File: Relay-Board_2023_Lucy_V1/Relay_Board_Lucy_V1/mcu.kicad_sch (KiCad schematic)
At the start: 34 parts, among them J6 SWD_HEADER, J7 USB_B_Micro, J8 Conn_02x14_Top_Bottom, J9 DE9_Receptacle_MountingHoles, SW1 PTS815 SJM 250 SMTR LFS, SW2 PTS815 SJM 250 SMTR LFS, U10 STM32F446RETx, U7 LD39050PU33R, U9 MCP2542FD-E/SN, X1 OXETDLJANF-8MHZ

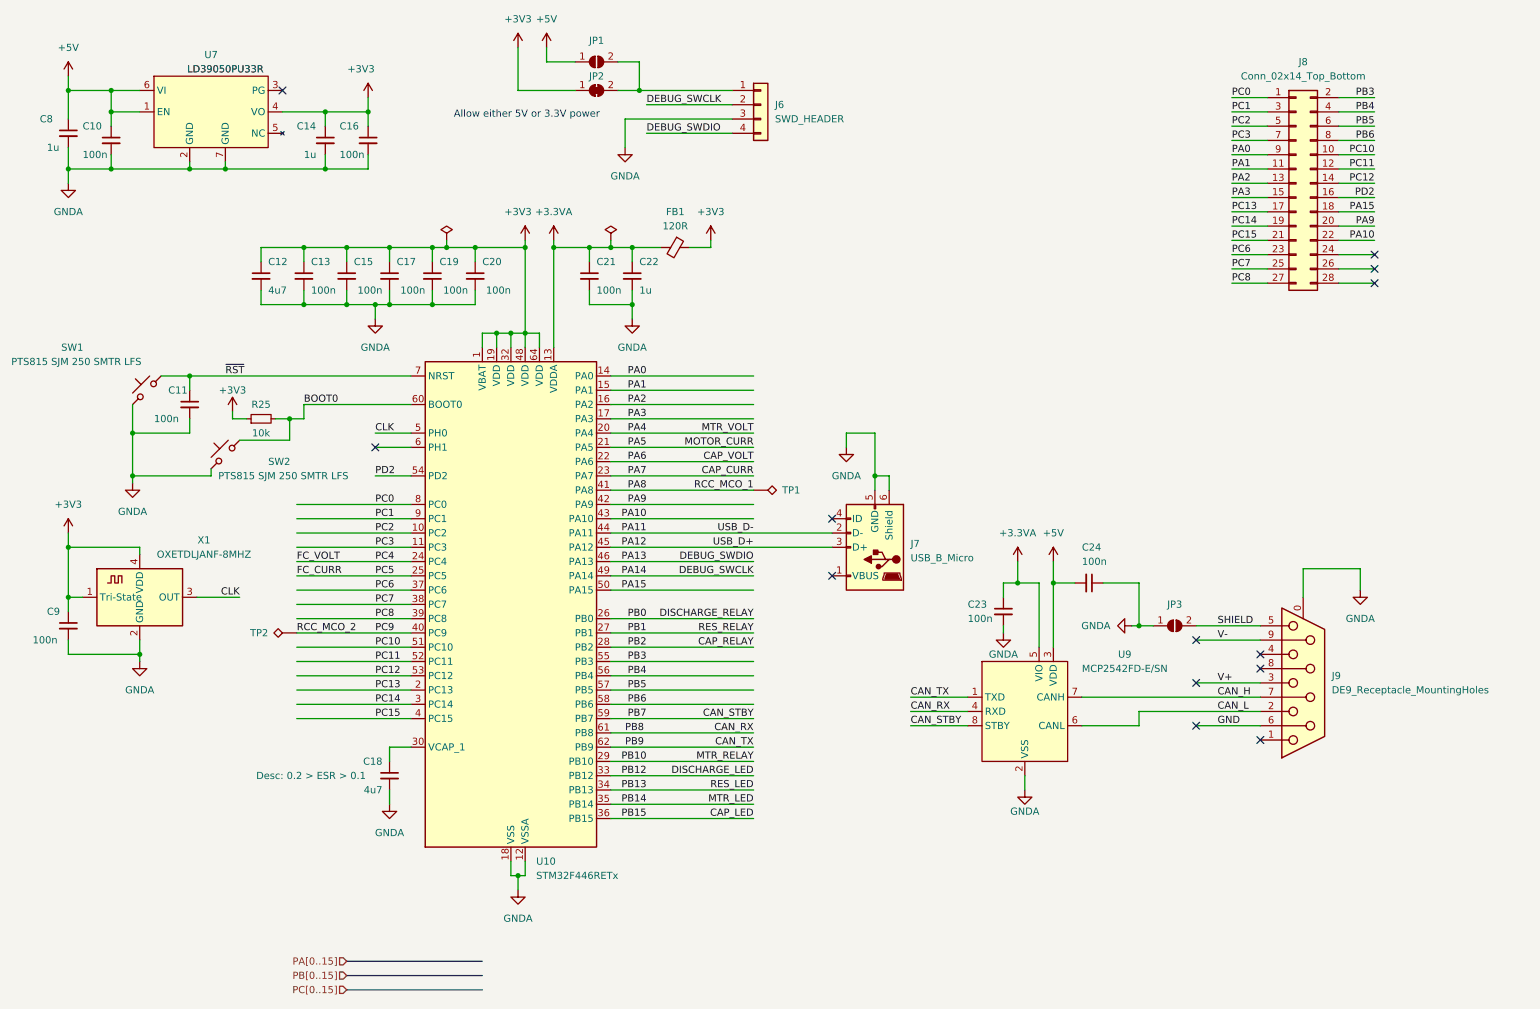
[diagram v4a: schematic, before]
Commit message: Board layout is done and routed
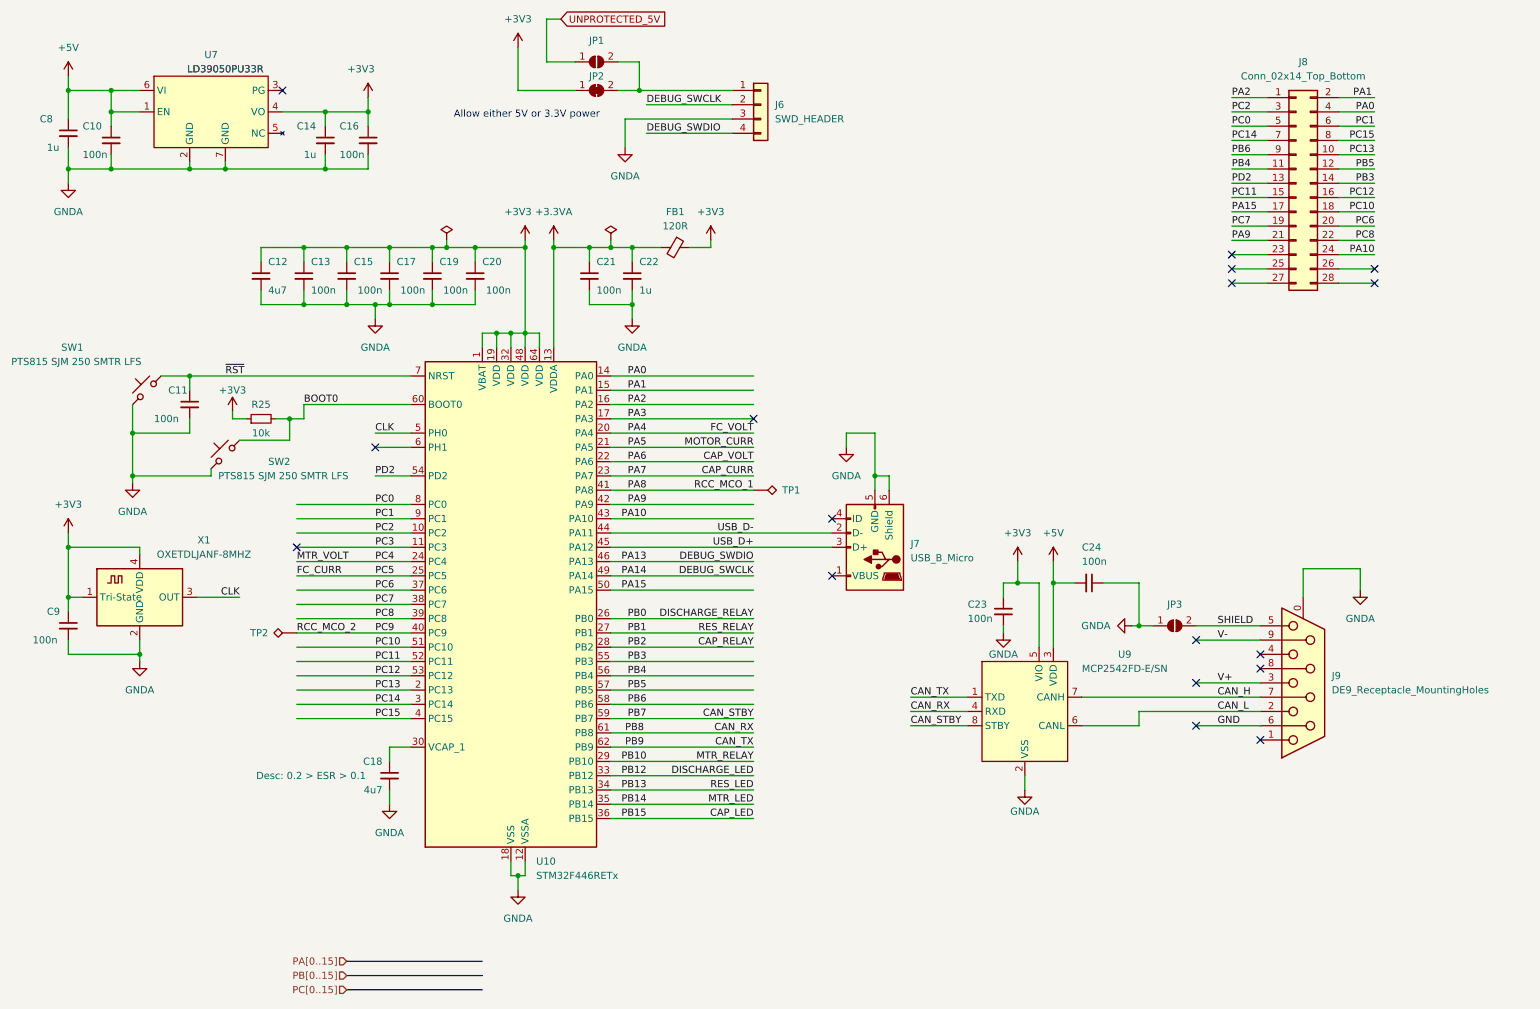
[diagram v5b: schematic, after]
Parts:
- SW2: footprint Inductor_SMD:L_1206_3216Metric -> Button_Switch_SMD:SW_SPST_PTS810
- TP1, TP2: footprint TestPoint:TestPoint_THTPad_D2.0mm_Drill1.0mm -> TestPoint:TestPoint_Pad_1.0x1.0mm
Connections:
- net +3.3VA: no longer C23.1, U9.5 (VIO)
- net +3V3: now also C23.1, U9.5 (VIO)
- net +5V: no longer JP1.1 (A)
- net FC_VOLT: now also U10.20 (PA4); no longer U10.24 (PC4)
- net MTR_VOLT: now also U10.24 (PC4); no longer U10.20 (PA4)
- net PA0: now also J8.4 (Pin_4); no longer J8.9 (Pin_9)
- net PA1: now also J8.2 (Pin_2); no longer J8.11 (Pin_11)
- net PA10: now also J8.24 (Pin_24); no longer J8.22 (Pin_22)
- net PA15: now also J8.17 (Pin_17); no longer J8.18 (Pin_18)
- net PA2: now also J8.1 (Pin_1); no longer J8.13 (Pin_13)
- net PA3: no longer J8.15 (Pin_15)
- net PA9: now also J8.21 (Pin_21); no longer J8.20 (Pin_20)
- net PB3: now also J8.14 (Pin_14); no longer J8.2 (Pin_2)
- net PB4: now also J8.11 (Pin_11); no longer J8.4 (Pin_4)
- net PB5: now also J8.12 (Pin_12); no longer J8.6 (Pin_6)
- net PB6: now also J8.9 (Pin_9); no longer J8.8 (Pin_8)
- net PC0: now also J8.5 (Pin_5); no longer J8.1 (Pin_1)
- net PC1: now also J8.6 (Pin_6); no longer J8.3 (Pin_3)
- net PC10: now also J8.18 (Pin_18); no longer J8.10 (Pin_10)
- net PC11: now also J8.15 (Pin_15); no longer J8.12 (Pin_12)
- net PC12: now also J8.16 (Pin_16); no longer J8.14 (Pin_14)
- net PC13: now also J8.10 (Pin_10); no longer J8.17 (Pin_17)
- net PC14: now also J8.7 (Pin_7); no longer J8.19 (Pin_19)
- net PC15: now also J8.8 (Pin_8); no longer J8.21 (Pin_21)
- net PC2: now also J8.3 (Pin_3); no longer J8.5 (Pin_5)
- net PC3: no longer J8.7 (Pin_7)
- net PC6: now also J8.20 (Pin_20); no longer J8.23 (Pin_23)
- net PC7: now also J8.19 (Pin_19); no longer J8.25 (Pin_25)
- net PC8: now also J8.22 (Pin_22); no longer J8.27 (Pin_27)
- net PD2: now also J8.13 (Pin_13); no longer J8.16 (Pin_16)
- net PA11 renamed USB_D-
- net PA12 renamed USB_D+
- new net UNPROTECTED_5V: JP1.1 (A)
- no-connect marks 13 -> 17

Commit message: $
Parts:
- added R34: 120, Resistor_SMD:R_0603_1608Metric, symbol Device:R_Small
- C18: Desc 0.2 > ESR > 0.1 -> ESR > 1
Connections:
- net CAN_H: now also R34.2
- net CAN_L: now also R34.1
- net GNDA: now also J8.25 (Pin_25), J8.27 (Pin_27)
- net UNPROTECTED_12V: now reaches J8.26 (Pin_26)
- net UNPROTECTED_12V: now also J8.28 (Pin_28)
- no-connect marks 17 -> 13
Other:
- moved on the sheet: C23

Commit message: Started work on the BOM file and I updated the lower current relays to work with 50A models
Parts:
- C10, C11, C13, C15, C16, C17, C19, C20, C21, C23, C24, C9: Part# (none) -> C88219
- C12: Part# (none) -> C108342
- C14, C22, C8: Part# (none) -> C77049
- C18, FB1, J7, J9: Part# (none) -> digikey
- J6, J8, JP1, JP2, JP3, TP1, TP2: Part# (none) -> N/A
- R25: Part# (none) -> C25804
- R34: Part# (none) -> C22787
- SW1, SW2: Part# (none) -> C2689510
- U10: Part# (none) -> C69336
- U7: Part# (none) -> C132827
- U9: Part# (none) -> C220598

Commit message: updated, created gerbers, created p&p, created BOM's
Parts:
- C18: Desc ESR > 1 -> ESR < 1; Part# digikey -> C108342
- FB1: value 120R -> 300R; Part# digikey -> 541-2283-1-ND
- J7: footprint Connector_USB:USB_Micro-B_Wuerth_629105150521 -> RB_FTP:USB_Micro-B_Wuerth_629105150521; Part# digikey -> 732-5960-1-ND
- J8, JP1, JP2: now left out of the parts list
- J9: Part# digikey -> N/A
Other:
- note added: "FB1: - 300 Ohms @ 100MHz - DCR 300 mOhms"
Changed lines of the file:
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@@
+    (effects (font (size 1.27 1.27)) (justify left bottom))
+  )
+  (text "FB1:\n - 300 Ohms @ 100MHz\n - DCR 300 mOhms" (at 134.62 66.04 0)
     (effects (font (size 1.27 1.27)) (justify left bottom))
   )
@@
   )
   (symbol (lib_id "Jumper:SolderJumper_2_Bridged") (at 120.65 27.94 0) (unit 1)
-    (in_bom yes) (on_board yes) (dnp no)
+    (in_bom no) (on_board yes) (dnp no)
     (property "Reference" "JP2" (at 120.65 25.4 0)
       (effects (font (size 1.27 1.27)))
@@
       (effects (font (size 1.27 1.27)) hide)
     )
-    (property "Part#" "digikey" (at 246.38 133.35 0)
+    (property "Part#" "N/A" (at 246.38 133.35 0)
       (effects (font (size 1.27 1.27)) hide)
     )
@@
       (effects (font (size 1.27 1.27)) hide)
     )
-    (property "Datasheet" "~" (at 83.82 149.86 0)
-      (effects (font (size 1.27 1.27)) hide)
-    )
-    (property "Part#" "digikey" (at 83.82 149.86 0)
-      (effects (font (size 1.27 1.27)) hide)
-    )
-    (property "Desc" "ESR > 1" (at 69.85 149.86 0) (show_name)
+    (property "Datasheet" "https://datasheet.lcsc.com/lcsc/2304140030_FH--Guangdong-Fenghua-Advanced-Tech-0603B475K100NT_C108342.pdf" (at 83.82 149.86 0)
+      (effects (font (size 1.27 1.27)) hide)
+    )
+    (property "Part#" "C108342" (at 83.82 149.86 0)
+      (effects (font (size 1.27 1.27)) hide)
+    )
+    (property "Desc" "ESR < 1" (at 71.12 149.86 0) (show_name)
       (effects (font (size 1.27 1.27)))
     )
@@
       (effects (font (size 1.27 1.27)) (justify right))
     )
-    (property "Footprint" "Connector_USB:USB_Micro-B_Wuerth_629105150521" (at 166.37 107.95 0)
-      (effects (font (size 1.27 1.27)) hide)
-    )
-    (property "Datasheet" "~" (at 166.37 107.95 0)
-      (effects (font (size 1.27 1.27)) hide)
-    )
-    (property "Part#" "digikey" (at 170.18 109.22 0)
+    (property "Footprint" "RB_FTP:USB_Micro-B_Wuerth_629105150521" (at 166.37 107.95 0)
+      (effects (font (size 1.27 1.27)) hide)
+    )
+    (property "Datasheet" "https://www.we-online.com/katalog/datasheet/629105150521.pdf" (at 166.37 107.95 0)
+      (effects (font (size 1.27 1.27)) hide)
+    )
+    (property "Part#" "732-5960-1-ND" (at 170.18 109.22 0)
       (effects (font (size 1.27 1.27)) hide)
     )
@@
   )
   (symbol (lib_id "Connector_Generic:Conn_02x14_Odd_Even") (at 245.11 44.45 0) (unit 1)
-    (in_bom yes) (on_board yes) (dnp no) (fields_autoplaced)
+    (in_bom no) (on_board yes) (dnp no) (fields_autoplaced)
     (property "Reference" "J8" (at 246.38 22.86 0)
       (effects (font (size 1.27 1.27)))
@@
   )
   (symbol (lib_id "Jumper:SolderJumper_2_Open") (at 120.65 22.86 0) (unit 1)
-    (in_bom yes) (on_board yes) (dnp no) (fields_autoplaced)
-    (property "Reference" "JP1" (at 120.65 19.05 0)
+    (in_bom no) (on_board yes) (dnp no)
+    (property "Reference" "JP1" (at 120.65 20.32 0)
       (effects (font (size 1.27 1.27)))
     )
@@
   )
   (symbol (lib_id "Device:FerriteBead_Small") (at 134.62 55.88 270) (unit 1)
-    (in_bom yes) (on_board yes) (dnp no) (fields_autoplaced)
+    (in_bom yes) (on_board yes) (dnp no)
     (property "Reference" "FB1" (at 134.6581 49.53 90)
       (effects (font (size 1.27 1.27)))
     )
-    (property "Value" "120R" (at 134.6581 52.07 90)
+    (property "Value" "300R" (at 134.62 52.07 90)
       (effects (font (size 1.27 1.27)))
     )
@@
       (effects (font (size 1.27 1.27)) hide)
     )
-    (property "Datasheet" "~" (at 134.62 55.88 0)
-      (effects (font (size 1.27 1.27)) hide)
-    )
-    (property "Part#" "digikey" (at 134.62 55.88 0)
-      (effects (font (size 1.27 1.27)) hide)
-    )
+    (property "Datasheet" "https://www.vishay.com/docs/34023/ilb1206.pdf" (at 134.62 55.88 0)
+      (effects (font (size 1.27 1.27)) hide)
+    )
+    (property "Part#" "541-2283-1-ND" (at 134.62 55.88 0)
+      (effects (font (size 1.27 1.27)) hide)
+    )
